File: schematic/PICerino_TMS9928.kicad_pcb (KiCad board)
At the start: 2 copper layers, 105 x 112.9 mm, 80 parts, among them CON1 PICERINO-EDGE, IC1 ADG453BNZ, J1 Conn_01x02, J10 Conn_01x08, J11 Conn_01x08, J12 Conn_01x03, J2 Y_Conn_01x02, J3 BY_Conn_01x02, J4 RY_Conn_01x02, J5 Conn_01x02, J6 Y_Conn_DC_FIX_01x02, J7 Conn_01x02, J8 Conn_01x02, J9 Conn_01x02, U1 LM1881, Y1 Crystal

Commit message: added two connectors to break out lm1881 outputs. essentially this is so outputs can be setup to particular use case. this is not a great video circuit, the routing is sloppy in this version.
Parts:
- added J13: Conn_01x02, Connector_PinHeader_2.54mm:PinHeader_1x02_P2.54mm_Vertical, F.Cu at (202.1, 50.4)
- added J14: Conn_01x02, Connector_PinHeader_2.54mm:PinHeader_1x02_P2.54mm_Vertical, F.Cu at (196.0, 61.5)
- moved C33 1.65 mm to (206.2, 66.9)
- moved C31 0.51 mm to (208.2, 53.7)
- moved R13 0.25 mm to (202.3, 70.5)
- moved C30 0.06 mm to (197.3, 67.4)
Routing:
- net Net-(J14-Pad1): track 0.00 -> 16.6 mm
- net Net-(J13-Pad2): track 0.00 -> 7.26 mm
- net Net-(J13-Pad1): track 0.00 -> 6.39 mm
- net Net-(IC1-Pad1): track 41.1 -> 38.1 mm, vias 4 -> 2
- net VCC: track 681.0 -> 683.3 mm
- net Net-(C9-Pad2): track 78.2 -> 79.1 mm
- net Net-(C31-Pad2): track 4.17 -> 3.53 mm
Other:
- board text added: "YDC"
- board text removed: "Y_DC"

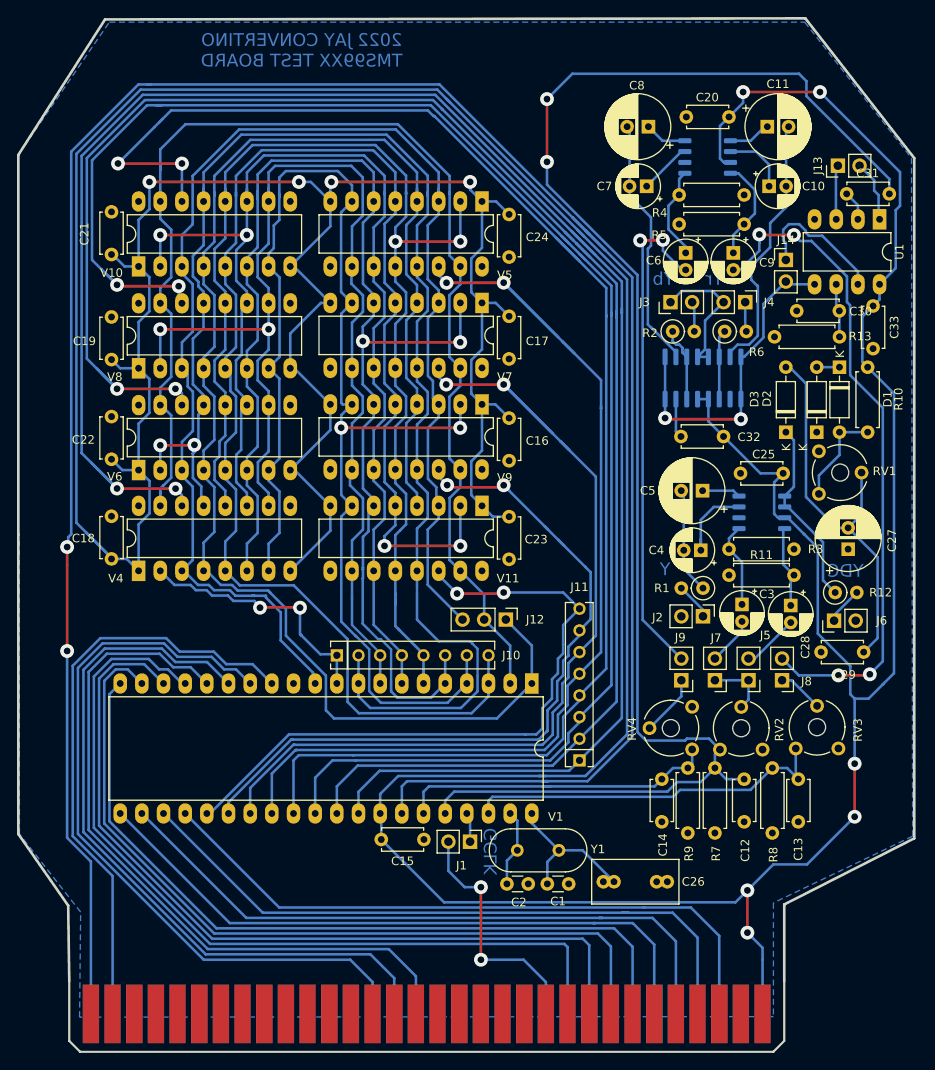
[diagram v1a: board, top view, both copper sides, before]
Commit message: major change to video circuit, first working version that does not suffer from over blue issue. This has only been tested to work with the retrotink x2. Since most YrYbY do not accept 240p and it needs to be upscaled. Values for the 2.7v DC bias zener diode circuit will be finalized soon when they arrive (makeshift circuit in use at the moment.. 5-3.3 oh yeah ;))
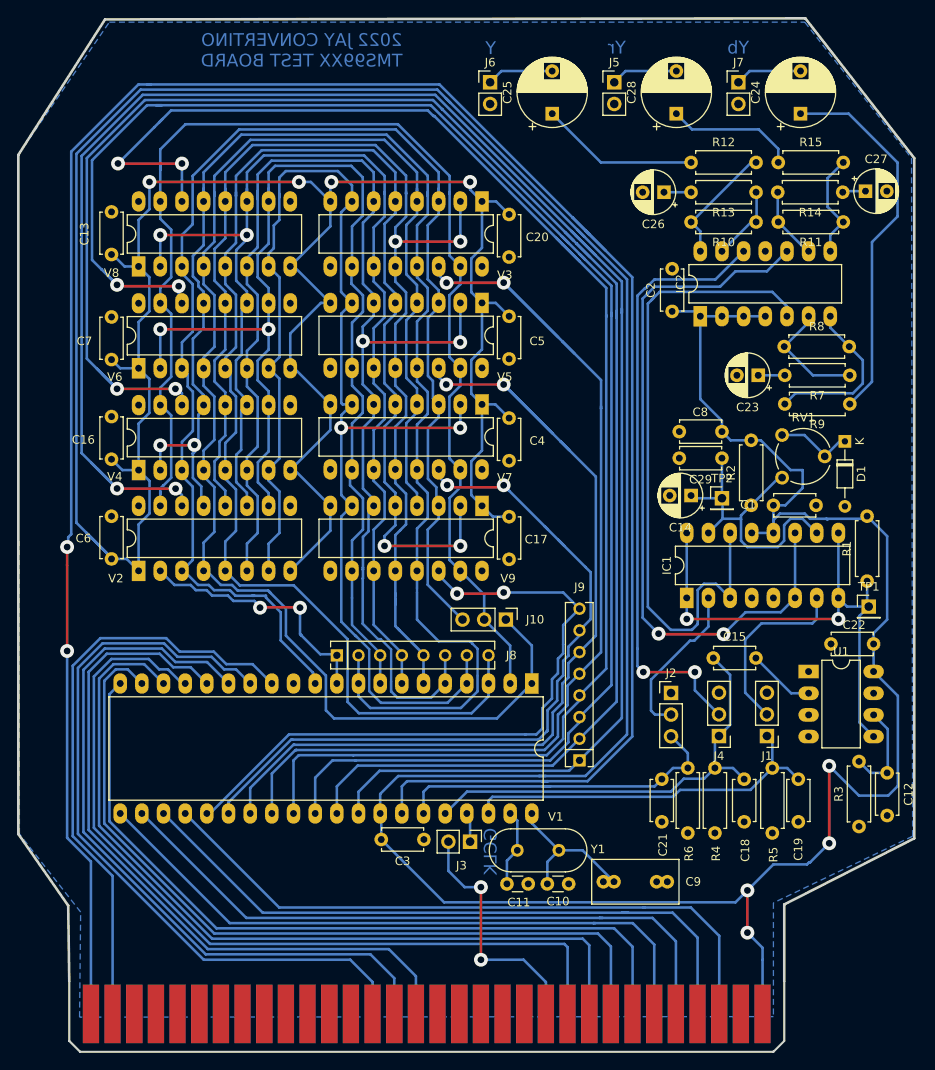
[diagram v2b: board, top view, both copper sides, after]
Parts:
- removed the C10 at (194.1, 52.8)
- removed the C11 at (193.8, 45.8)
- removed the C3 at (190.9, 101.9)
- removed C30, C31: 100nF, Capacitor_THT:C_Disc_D4.7mm_W2.5mm_P5.00mm
- removed the C4 at (186.1, 95.5)
- removed the C5 at (186.3, 88.5)
- removed the C6 at (184.3, 60.6)
- removed the C7 at (179.7, 52.8)
- removed the C8 at (179.9, 45.8)
- removed the C9 at (189.9, 60.6)
- removed D2, D3: 1N914, Diode_THT:D_DO-35_SOD27_P7.62mm_Horizontal
- removed J13, J14: Conn_01x02, Connector_PinHeader_2.54mm:PinHeader_1x02_P2.54mm_Vertical
- removed the J3 at (182.5, 66.4)
- removed the J8 at (195.6, 110.7)
- removed the J9 at (183.8, 110.7)
- removed the R4 at (183.5, 53.8)
- removed the R5 at (183.5, 57.3)
- removed the R6 at (188.8, 69.8)
- removed RV2, RV3, RV4: 10K, Potentiometer_THT:Potentiometer_Piher_PT-6-V_Vertical_Hole
- removed the V2 at (193.2, 91.1)
- removed the V3 at (186.9, 49.4)
- added C12: 100nF, Capacitor_THT:C_Disc_D4.7mm_W2.5mm_P5.00mm, F.Cu at (207.9, 121.6)
- added C14: 10uF, Capacitor_THT:CP_Radial_D5.0mm_P2.50mm, F.Cu at (184.9, 89.1)
- added C15: 100nF, Capacitor_THT:C_Disc_D4.7mm_W2.5mm_P5.00mm, F.Cu at (187.5, 108.1)
- added C23: 33uF, Capacitor_THT:CP_Radial_D5.0mm_P2.50mm, F.Cu at (192.8, 75.0)
- added C24: 470uF, Capacitor_THT:CP_Radial_D8.0mm_P5.00mm, F.Cu at (197.7, 44.3)
- added C25: 470uF, Capacitor_THT:CP_Radial_D8.0mm_P5.00mm, F.Cu at (168.6, 44.3)
- added C26: 33uF, Capacitor_THT:CP_Radial_D5.0mm_P2.50mm, F.Cu at (181.7, 53.5)
- added IC2: AD813ANZ, Package_DIP:DIP-14_W7.62mm_LongPads, F.Cu at (186.0, 68.1)
- added J1: Conn_01x03, Connector_PinHeader_2.54mm:PinHeader_1x03_P2.54mm_Vertical, F.Cu at (193.8, 117.3)
- added R14: 510R, Resistor_THT:R_Axial_DIN0207_L6.3mm_D2.5mm_P7.62mm_Horizontal, F.Cu at (202.7, 53.5)
- added R15: 75R, Resistor_THT:R_Axial_DIN0207_L6.3mm_D2.5mm_P7.62mm_Horizontal, F.Cu at (195.1, 50.0)
- added R7: 510R, Resistor_THT:R_Axial_DIN0207_L6.3mm_D2.5mm_P7.62mm_Horizontal, F.Cu at (203.5, 75.0)
- added R8: 510R, Resistor_THT:R_Axial_DIN0207_L6.3mm_D2.5mm_P7.62mm_Horizontal, F.Cu at (195.8, 71.6)
- added R9: 75R, Resistor_THT:R_Axial_DIN0207_L6.3mm_D2.5mm_P7.62mm_Horizontal, F.Cu at (203.5, 78.4)
- added TP1: TestPoint, Connector_PinHeader_2.54mm:PinHeader_1x01_P2.54mm_Vertical, F.Cu at (205.7, 102.1)
- added TP2: TestPoint, Connector_PinHeader_2.54mm:PinHeader_1x01_P2.54mm_Vertical, F.Cu at (188.5, 89.4)
- C27: value 100uF -> 33uF; footprint Capacitor_THT:CP_Radial_D7.5mm_P2.50mm -> Capacitor_THT:CP_Radial_D5.0mm_P2.50mm
- C28: value 10uF -> 470uF; footprint Capacitor_THT:CP_Radial_D5.0mm_P2.00mm -> Capacitor_THT:CP_Radial_D8.0mm_P5.00mm
- D1: value 1N914 -> D_Zener_2-7; footprint Diode_THT:D_DO-35_SOD27_P7.62mm_Horizontal -> Diode_THT:D_DO-34_SOD68_P7.62mm_Horizontal
- IC1: value ADG453BNZ -> ADG453/413; footprint Package_SO:SOIC-16_3.9x9.9mm_P1.27mm -> Package_DIP:DIP-16_W7.62mm_LongPads; moved to F.Cu
- J2: value Y_Conn_01x02 -> Conn_01x03; footprint Connector_PinHeader_2.54mm:PinHeader_1x02_P2.54mm_Vertical -> Connector_PinHeader_2.54mm:PinHeader_1x03_P2.54mm_Vertical
- J4: value RY_Conn_01x02 -> Conn_01x03; footprint Connector_PinHeader_2.54mm:PinHeader_1x02_P2.54mm_Vertical -> Connector_PinHeader_2.54mm:PinHeader_1x03_P2.54mm_Vertical
- J5: value Conn_01x02 -> Conn_01x02_Yr
- J6: value Y_Conn_DC_FIX_01x02 -> Conn_01x02_Y
- J7: value Conn_01x02 -> Conn_01x02_Yb
- R1: value 75R -> 1K; footprint Resistor_THT:R_Axial_DIN0207_L6.3mm_D2.5mm_P2.54mm_Vertical -> Resistor_THT:R_Axial_DIN0207_L6.3mm_D2.5mm_P7.62mm_Horizontal
- R10: value 470R -> 510R
- R11: value 1M -> 510R
- R12: footprint Resistor_THT:R_Axial_DIN0207_L6.3mm_D2.5mm_P2.54mm_Vertical -> Resistor_THT:R_Axial_DIN0207_L6.3mm_D2.5mm_P7.62mm_Horizontal
- R13: value 680K -> 510R
- R2: value 75R -> 470R; footprint Resistor_THT:R_Axial_DIN0207_L6.3mm_D2.5mm_P2.54mm_Vertical -> Resistor_THT:R_Axial_DIN0207_L6.3mm_D2.5mm_P7.62mm_Horizontal
- R3: value 1M -> 680k
- RV1: value 100R -> R_POT; footprint Potentiometer_THT:Potentiometer_Piher_PT-6-V_Vertical_Hole -> Potentiometer_THT:Potentiometer_Piher_PT-6-V_Vertical
- moved J6 74.9 mm to (161.4, 40.6), turned to 0 degrees
- moved J5 71.8 mm to (175.9, 40.6), turned to 0 degrees
- moved J7 70.2 mm to (190.5, 40.6), turned to 0 degrees
- moved C28 59.2 mm to (183.2, 44.3), turned to 90 degrees
- moved U1 53.7 mm to (198.7, 109.7), turned to 0 degrees
- moved R12 53.2 mm to (184.9, 50.0)
- moved J4 51.0 mm to (188.2, 117.3), turned to 180 degrees
- moved R11 43.5 mm to (202.8, 57.0), turned to 180 degrees
- moved C27 42.0 mm to (205.4, 53.4), turned to 0 degrees
- moved C8 36.9 mm to (188.5, 81.6)
- moved R3 33.4 mm to (204.6, 127.9), turned to 90 degrees
- moved IC1 25.9 mm to (184.4, 101.1), turned to 90 degrees
- moved C29 25.5 mm to (188.5, 84.7), turned to 180 degrees
- moved C2 23.6 mm to (182.7, 67.5), turned to 90 degrees
- moved C22 22.6 mm to (206.3, 106.5)
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- renumbered C32 to C1, C1 to C10, C2 to C11, C21 to C13, C22 to C16, C23 to C17, C12 to C18, C13 to C19, C33 to C2, C24 to C20, C14 to C21, C25 to C22, C15 to C3, C16 to C4, C17 to C5, C18 to C6, C19 to C7, C20 to C8, C26 to C9, J12 to J10, J1 to J3, J10 to J8, J11 to J9, R7 to R4, R8 to R5, R9 to R6, V4 to V2, V5 to V3, V6 to V4, V7 to V5, V8 to V6, V9 to V7, V10 to V8, V11 to V9
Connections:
- C27 pad 1: VSS -> Net-(C27-Pad1)
- C27 pad 2: Net-(C27-Pad2) -> VSS
- C29 pad 1: VSS -> Net-(C14-Pad1)
- C29 pad 2: Net-(C27-Pad2) -> VSS
- D1 pad 2: Net-(D1-Pad2) -> VSS
- IC1 pad 10: VSS -> Net-(C14-Pad1)
- IC1 pad 15: VSS -> Net-(C14-Pad1)
- IC1 pad 2: Net-(C7-Pad2) -> Net-(IC1-Pad2)
- J2 pad 1: Net-(J2-Pad1) -> VSS
- J2 pad 2: VSS -> Net-(IC1-Pad2)
- J4 pad 1: Net-(J4-Pad1) -> /Y
- J4 pad 2: VSS -> Net-(IC2-Pad12)
- J5 pad 1: Net-(J5-Pad1) -> Net-(C28-Pad2)
- J5 pad 2: Net-(C28-Pad2) -> VSS
- J6 pad 1: Net-(J6-Pad1) -> Net-(C25-Pad2)
- J7 pad 1: Net-(J5-Pad1) -> Net-(C24-Pad2)
- J7 pad 2: Net-(C3-Pad2) -> VSS
- R1 pad 1: Net-(C4-Pad2) -> Net-(IC1-Pad1)
- R1 pad 2: Net-(J2-Pad1) -> VCC
- R10 pad 1: VCC -> Net-(IC2-Pad13)
- R10 pad 2: Net-(D1-Pad2) -> Net-(IC2-Pad14)
- R11 pad 1: VSS -> Net-(IC2-Pad8)
- R11 pad 2: Net-(C28-Pad1) -> Net-(IC2-Pad9)
- R12 pad 2: Net-(J6-Pad1) -> Net-(IC2-Pad14)
- R13 pad 1: Net-(C30-Pad2) -> Net-(IC2-Pad13)
- R13 pad 2: VSS -> Net-(C26-Pad1)
- R2 pad 1: Net-(IC1-Pad14) -> Net-(C14-Pad1)
- R2 pad 2: Net-(J3-Pad2) -> VCC
- R3 pad 2: Net-(C3-Pad1) -> Net-(C12-Pad1)
- RV1 pad 1: Net-(D1-Pad2) -> Net-(C14-Pad1)
- RV1 pad 2: Net-(C27-Pad2) -> Net-(D1-Pad1)
- RV1 pad 3: VSS -> Net-(D1-Pad1)
- U1 pad 6: Net-(C30-Pad2) -> Net-(C12-Pad1)
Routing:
- net /Y: track 180.0 -> 52.3 mm, vias 2 -> 0
- net Net-(C9-Pad2): track 79.1 -> 0.00 mm, vias 4 -> 0
- net Net-(IC1-Pad11): track 8.20 -> 84.9 mm, vias 0 -> 2
- net Net-(IC2-Pad12): track 0.00 -> 71.3 mm, vias 0 -> 2
- net Net-(IC1-Pad14): track 8.84 -> 79.4 mm
- net Net-(C6-Pad2): track 58.6 -> 0.00 mm, vias 2 -> 0
- net VCC: track 683.3 -> 634.6 mm, vias 10 -> 8
- net Net-(C27-Pad2): track 46.7 -> 0.00 mm
- net Net-(C24-Pad1): track 0.00 -> 44.4 mm
- net Net-(C14-Pad1): track 0.00 -> 38.1 mm
- net Net-(C7-Pad2): track 29.7 -> 0.00 mm
- net Net-(IC1-Pad1): track 38.1 -> 61.4 mm
- net VSS: track 50.2 -> 29.0 mm
- net Net-(IC2-Pad7): track 0.00 -> 19.6 mm
- net Net-(IC1-Pad2): track 0.00 -> 18.8 mm
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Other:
- board text removed: "YDC"

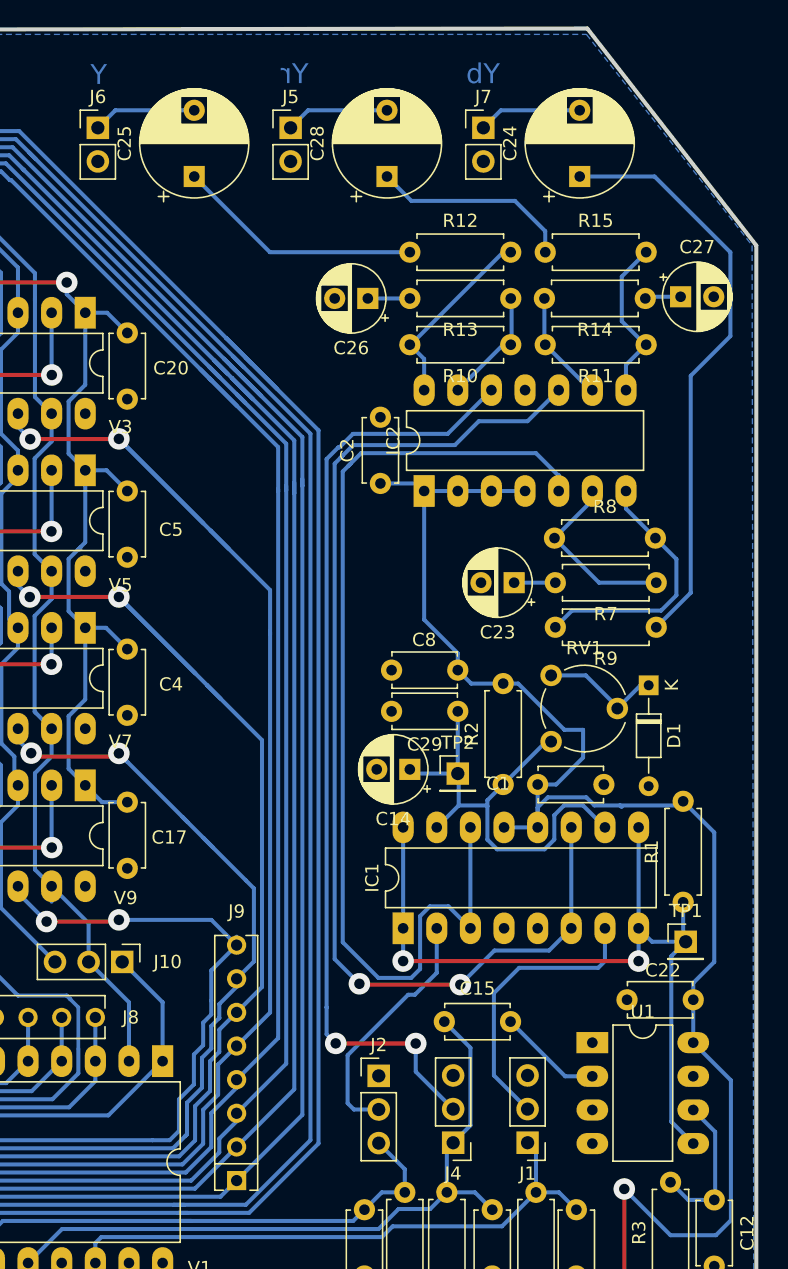
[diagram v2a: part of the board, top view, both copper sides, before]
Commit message: added a bleader resistor, still need to test the circuit before creating final board.
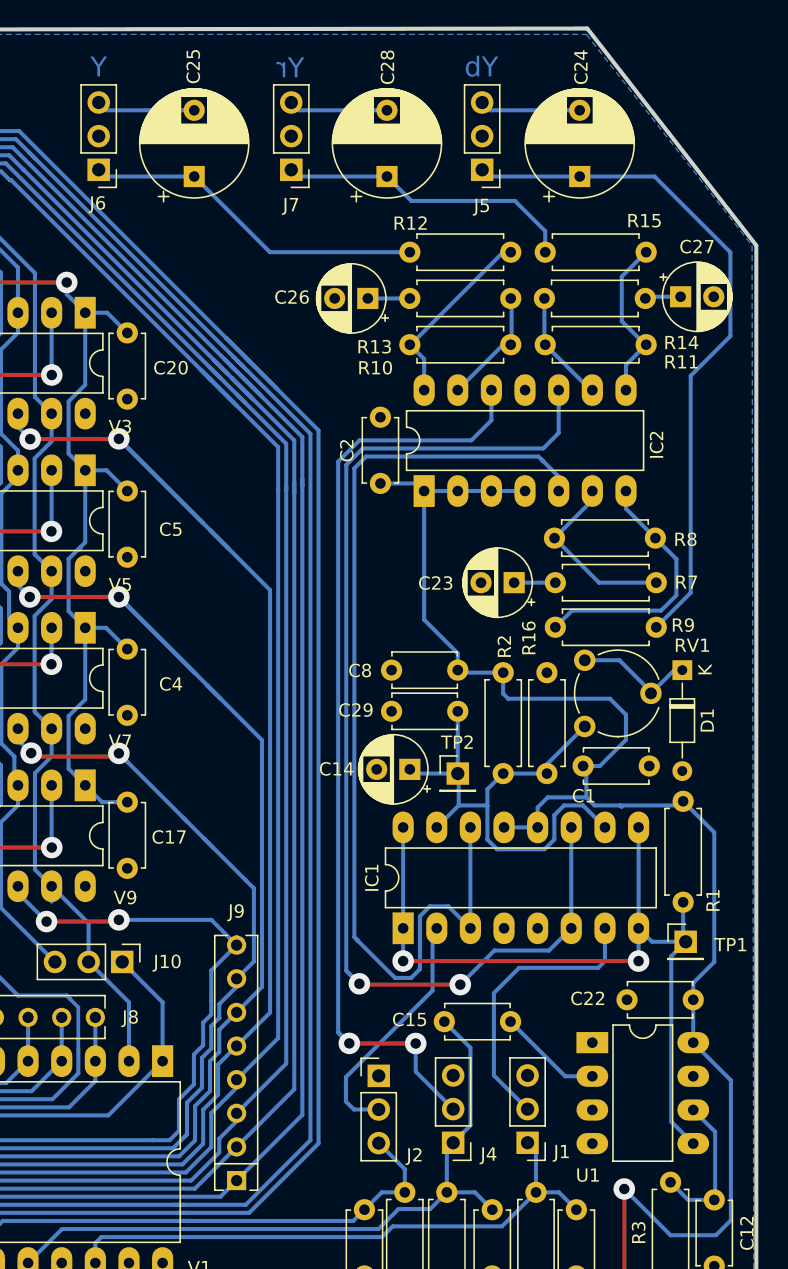
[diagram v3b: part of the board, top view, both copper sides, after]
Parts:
- added R16: 1M, Resistor_THT:R_Axial_DIN0207_L6.3mm_D2.5mm_P7.62mm_Horizontal, F.Cu at (195.3, 81.8)
- J5: value Conn_01x02_Yr -> Conn_01x03_Yb; footprint Connector_PinHeader_2.54mm:PinHeader_1x02_P2.54mm_Vertical -> Connector_PinHeader_2.54mm:PinHeader_1x03_P2.54mm_Vertical
- J6: value Conn_01x02_Y -> Conn_01x03_Y; footprint Connector_PinHeader_2.54mm:PinHeader_1x02_P2.54mm_Vertical -> Connector_PinHeader_2.54mm:PinHeader_1x03_P2.54mm_Vertical
- J7: value Conn_01x02_Yb -> Conn_01x03_Yr; footprint Connector_PinHeader_2.54mm:PinHeader_1x02_P2.54mm_Vertical -> Connector_PinHeader_2.54mm:PinHeader_1x03_P2.54mm_Vertical
- moved J7 14.8 mm to (176.0, 43.8), turned to 180 degrees
- moved J5 14.8 mm to (190.4, 43.8), turned to 180 degrees
- moved C1 3.70 mm to (198.0, 88.8)
- moved J6 3.17 mm to (161.4, 43.8), turned to 180 degrees
- moved D1 2.79 mm to (205.5, 81.6)
- moved RV1 2.79 mm to (198.1, 85.9)
- moved R2 0.83 mm to (192.0, 89.4)
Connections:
- J5 pad 1: Net-(C28-Pad2) -> Net-(C24-Pad1)
- J6 pad 1: Net-(C25-Pad2) -> Net-(C25-Pad1)
- J7 pad 1: Net-(C24-Pad2) -> Net-(C28-Pad1)
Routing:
- net Net-(C24-Pad1): track 44.4 -> 52.0 mm
- net Net-(C28-Pad1): track 15.2 -> 22.7 mm
- net Net-(C25-Pad1): track 18.6 -> 26.1 mm
- net Net-(C14-Pad1): track 38.1 -> 42.4 mm
- net Net-(IC1-Pad14): track 79.4 -> 76.3 mm
- net VCC: track 634.6 -> 637.1 mm
- net Net-(IC1-Pad11): track 84.9 -> 86.5 mm
- net Net-(IC2-Pad12): track 71.3 -> 71.9 mm

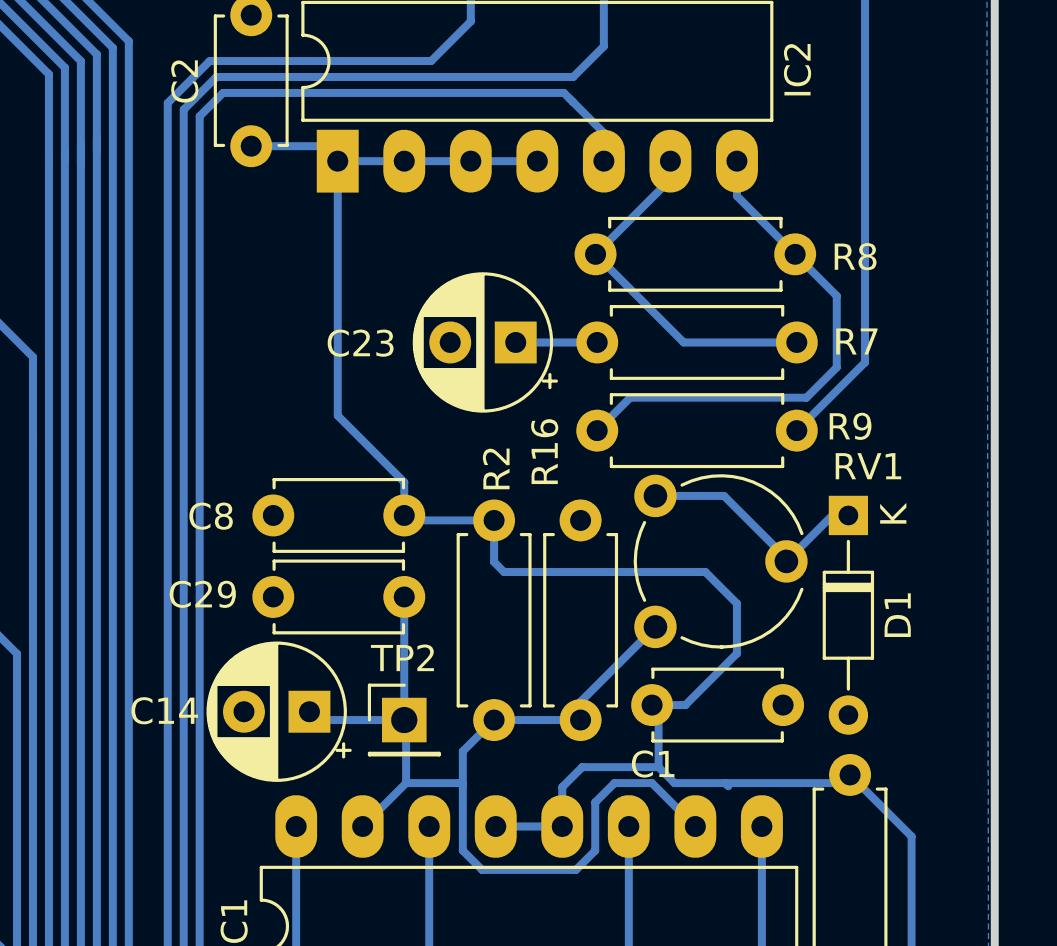
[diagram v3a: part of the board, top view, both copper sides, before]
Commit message: updated board to new zener diode bias design. After testing this provided the best adjustment range. Could use some more work to simply it and check failure conditions.
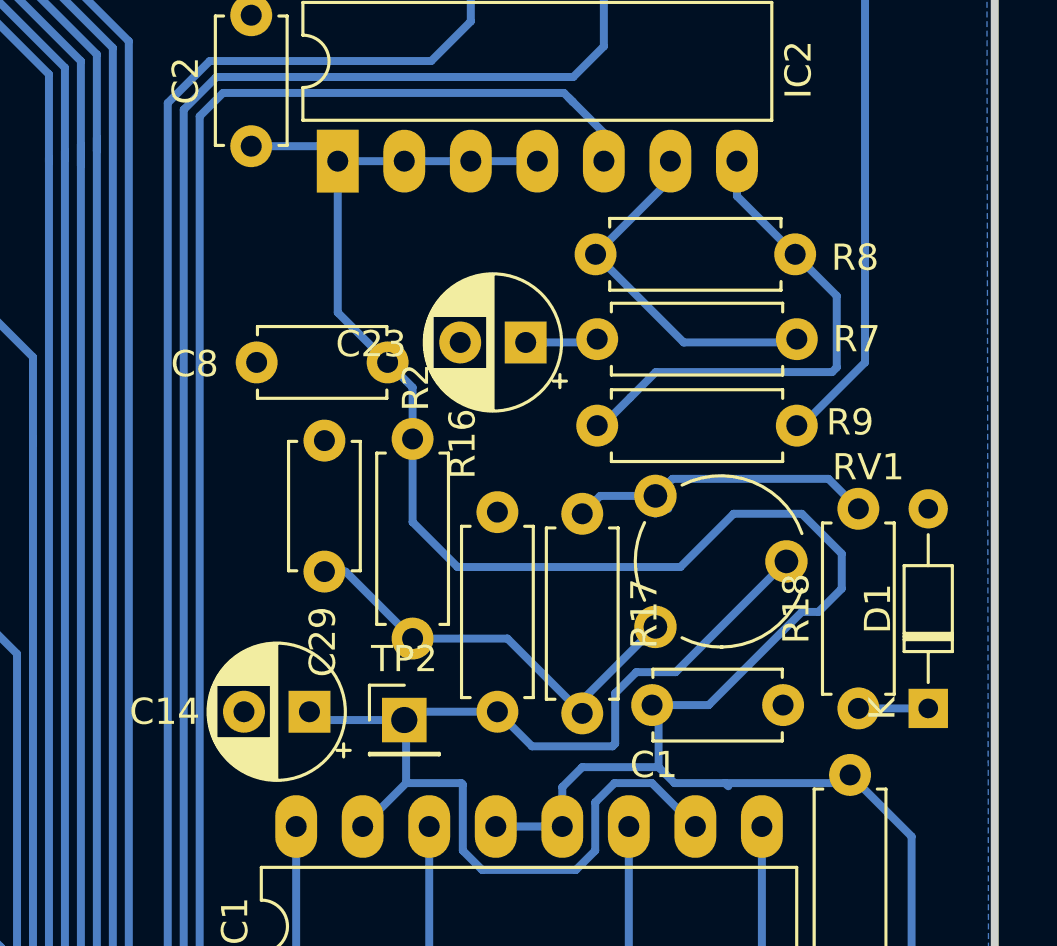
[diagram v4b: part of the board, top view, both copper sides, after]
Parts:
- added R17: 10R, Resistor_THT:R_Axial_DIN0207_L6.3mm_D2.5mm_P7.62mm_Horizontal, F.Cu at (195.3, 81.5)
- added R18: 2R2, Resistor_THT:R_Axial_DIN0207_L6.3mm_D2.5mm_P7.62mm_Horizontal, F.Cu at (205.9, 89.0)
- R16: value 1M -> 47K
- R2: value 470R -> 120R
- RV1: value R_POT -> 100R
- moved D1 7.97 mm to (208.5, 89.0), turned to 90 degrees
- moved C29 6.70 mm to (185.5, 78.7), turned to 270 degrees
- moved C8 5.88 mm to (187.9, 75.8)
- moved R2 4.40 mm to (188.8, 86.3)
- moved R16 3.19 mm to (192.1, 81.5)
- moved C23 0.38 mm to (193.2, 75.0)
- moved R9 0.19 mm to (203.5, 78.2)
- moved R7 0.13 mm to (203.5, 74.9)
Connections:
- C29 pad 1: Net-(C14-Pad1) -> VSS
- C29 pad 2: VSS -> Net-(C29-Pad2)
- R2 pad 1: Net-(C14-Pad1) -> Net-(C29-Pad2)
- RV1 pad 1: Net-(C14-Pad1) -> Net-(C29-Pad2)
- RV1 pad 2: Net-(D1-Pad1) -> Net-(C14-Pad1)
- RV1 pad 3: Net-(D1-Pad1) -> Net-(R17-Pad1)
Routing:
- net Net-(C29-Pad2): track 0.00 -> 16.9 mm
- net Net-(R17-Pad1): track 0.00 -> 13.0 mm
- net VCC: track 637.1 -> 645.5 mm
- net Net-(D1-Pad1): track 9.20 -> 2.67 mm
- net Net-(C14-Pad1): track 42.4 -> 45.7 mm
